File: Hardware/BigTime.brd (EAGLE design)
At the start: 19 parts, among them U2 ATMEGA328P_TQFP, Y1 32.768kHz

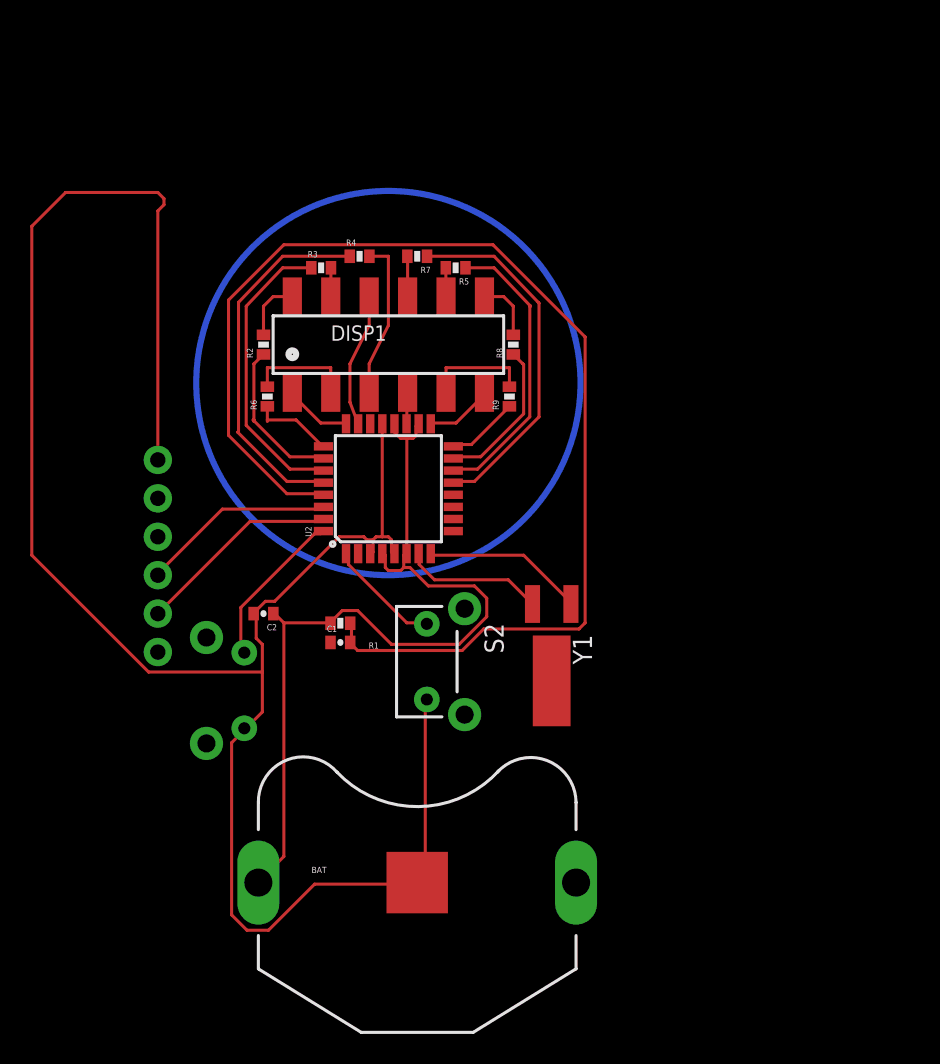
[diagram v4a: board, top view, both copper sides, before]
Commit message: fit 1" footprint
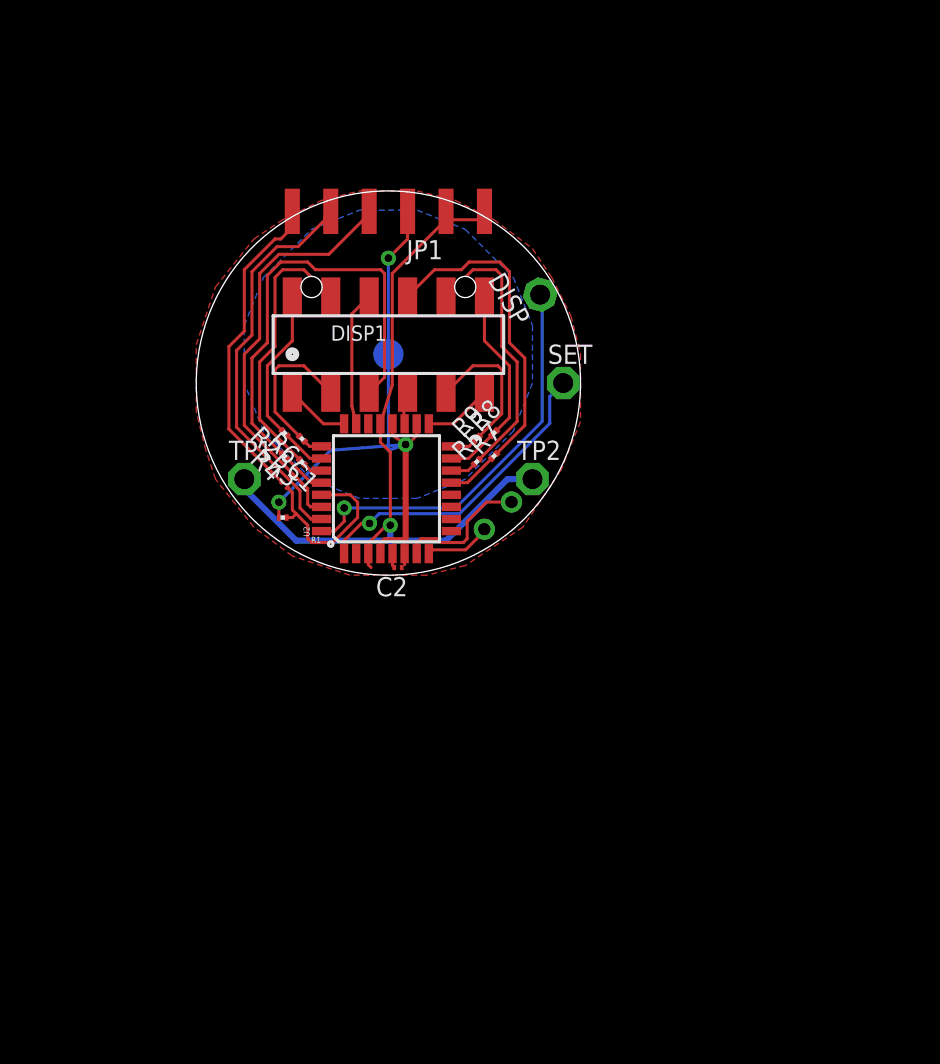
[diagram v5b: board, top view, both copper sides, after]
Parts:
- removed BAT: (no value), SparkFun-Electromechanical:BATTERY_20MM_PTH_COMPACT
- removed S1, S2: BUTTON, SparkFun-Electromechanical:TACTILE-PTH-SIDEEZ
- added DISP, SET: TPPAD1-13, testpad:P1-13
- added TP1, TP2: PTR1PAD1-13, testpad:P1-13
- added VCC: TPTP20R, testpad:TP20R
- C1, C2: device SparkFun-Passives:0402-CAP -> resistor:C0201
- JP1: value FTDI_BASICPTH -> (none); device SparkFun:FTDI_BASIC -> SparkFun-Connectors:1X06-SMD
- R1, R2, R3, R4, R5, R6, R7, R8, R9: device SparkFun-Passives:0402-RES -> resistor:R0201
- Y1: device SparkFun-FreqCtrl:CRYSTAL-32KHZ-SMD -> crystal:TC26H
- moved JP1 28.5 mm to (15.2, 41.9), flipped to the top, turned to 0 degrees
- moved R7 14.2 mm to (22.2, 30.7), turned to 45 degrees
- moved R4 14.1 mm to (8.38, 30.7), turned to 135 degrees
- moved R5 12.9 mm to (21.1, 30.4), turned to 45 degrees
- moved R3 12.9 mm to (9.53, 30.4), turned to 135 degrees
- moved C1 11.0 mm to (8.38, 28.8), turned to 315 degrees
- moved C2 9.40 mm to (15.9, 23.4)
- moved R1 7.96 mm to (8.26, 26.7)
- moved Y1 6.84 mm to (22.5, 26.8), flipped to the bottom, turned to 315 degrees
- moved R2 6.01 mm to (8.38, 32.3), turned to 135 degrees
- moved R8 5.98 mm to (22.2, 32.3), turned to 45 degrees
- moved R6 3.61 mm to (9.53, 31.9), turned to 135 degrees
- moved R9 3.53 mm to (21.1, 31.9), turned to 45 degrees
- moved U2 0.13 mm to (15.1, 28.6)
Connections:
- net BTN: now also DISP.TP; no longer S1.1
- net GND: now also JP1.5, JP1.6, TP1.TP, TP2.TP; no longer BAT.2, JP1.GND, S1.2, S2.2
- net N$1: now also Y1.2; no longer Y1.X1
- net N$2: now also Y1.1; no longer Y1.X2
- net N$3: now also JP1.1; no longer JP1.DTR
- net RXI: now also JP1.3; no longer JP1.TXO
- net SET: now also SET.TP; no longer S2.1
- net TXO: now also JP1.2; no longer JP1.RXI
- net VCC: now also JP1.4, VCC.TP; no longer BAT.1
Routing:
- net GND: track 136.1 -> 53.9 mm, vias 0 -> 1
- net RST: track 81.2 -> 12.4 mm
- net C: track 24.3 -> 2.91 mm
- net N$3: track 0.00 -> 21.3 mm
- net F: track 23.7 -> 3.29 mm
- net N$6: track 10.6 -> 29.7 mm
- net N$9: track 2.67 -> 21.1 mm
- net B: track 19.6 -> 1.28 mm
- net D: track 19.3 -> 1.66 mm
- net N$7: track 1.91 -> 18.2 mm
- net N$5: track 1.91 -> 18.1 mm
- net BTN: track 10.6 -> 26.5 mm, vias 0 -> 1
- net RXI: track 12.9 -> 27.4 mm
- net VCC: track 56.0 -> 42.4 mm, vias 0 -> 3
- net SET: track 7.60 -> 20.7 mm, vias 0 -> 1
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- added copper zone on layer 1, net GND
- added copper zone on layer 16, net VCC
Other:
- board outline added: 25.4 x 25.4 mm

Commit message: fit
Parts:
- removed DISP, SET: TPPAD1-13, testpad:P1-13
- removed TP1, TP2: PTR1PAD1-13, testpad:P1-13
- removed U$2: CREATIVE_COMMONS, SparkFun:CREATIVE_COMMONS
- removed VCC: TPTP20R, testpad:TP20R
- added BAT+: TPTP20R, testpad:TP20R
- added TP3, TP4: (no value), SparkFun-Connectors:1X01
- added TP5, TP6: (no value), adafruit:1X01-CLEANBIG
- DISP1: device SparkFun-Displays:DIL12_SM -> BigTime:DIL12_SM
- JP1: value (none) -> FTDI_DEVICERA_SMT; device SparkFun-Connectors:1X06-SMD -> BigTime:FTDI_DEVICE_RA_SMT
- Y1: device crystal:TC26H -> BigTime:TC26H
- moved Y1 19.8 mm to (20.8, 7.11), turned to 270 degrees
- moved DISP1 19.1 mm to (14.6, 19.1)
- moved U2 19.1 mm to (14.5, 9.53)
- moved R8 18.5 mm to (21.1, 13.8), turned to 90 degrees
- moved R2 18.4 mm to (8.13, 13.8), turned to 90 degrees
- moved R9 18.2 mm to (18.4, 13.8), turned to 90 degrees
- moved R6 18.1 mm to (10.8, 13.8), turned to 90 degrees
- moved R7 17.2 mm to (19.2, 13.8), turned to 90 degrees
- moved R4 17.0 mm to (10.0, 13.8), turned to 90 degrees
- moved R5 16.5 mm to (19.9, 13.8), turned to 90 degrees
- moved R3 16.5 mm to (9.27, 13.8), turned to 90 degrees
- moved C1 16.4 mm to (6.60, 12.6), turned to 270 degrees
- moved JP1 15.3 mm to (14.6, 26.7)
- moved R1 14.3 mm to (5.97, 12.6), turned to 90 degrees
- moved C2 1.53 mm to (16.0, 24.9), turned to 0 degrees
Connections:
- net A: now also U2.28; no longer U2.26
- net B: now also U2.26; no longer U2.27
- net BTN: now also TP3.1; no longer DISP.TP
- net C: now also U2.25; no longer U2.28
- net D: now also U2.15; no longer U2.14
- net DIG1: now also U2.27; no longer U2.24
- net DIG4: now also U2.14; no longer U2.17
- net DP: now also U2.17; no longer U2.16
- net E: now also U2.24; no longer U2.25
- net F: now also U2.16; no longer U2.13
- net G: now also U2.13; no longer U2.15
- net GND: now also TP5.1, TP6.1; no longer TP1.TP, TP2.TP
- net RXI: now also JP1.2; no longer JP1.3
- net SET: now also TP4.1; no longer SET.TP
- net TXO: now also JP1.3; no longer JP1.2
- net VCC: now also BAT+.TP; no longer VCC.TP
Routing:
- net N$9: track 21.1 -> 10.8 mm
- net N$7: track 18.2 -> 8.76 mm
- net N$5: track 18.1 -> 8.76 mm
- net N$8: track 9.58 -> 1.78 mm
- net N$11: track 9.53 -> 1.78 mm
- net N$6: track 29.7 -> 22.3 mm
- net VCC: track 42.4 -> 49.4 mm
- net N$3: track 21.3 -> 15.4 mm
- net GND: track 53.9 -> 59.1 mm
- net RST: track 12.4 -> 16.7 mm
- net RXI: track 27.4 -> 24.5 mm
- net TXO: track 26.5 -> 23.6 mm
- net DIG1: track 4.28 -> 6.30 mm
- net A: track 2.88 -> 4.84 mm
- net DIG4: track 4.53 -> 6.40 mm
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- added copper zone on layer 16, net GND
